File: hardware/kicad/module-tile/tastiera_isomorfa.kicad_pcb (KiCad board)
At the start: 2 copper layers, 63 parts, among them J101 Conn_LEFT, J102 Conn_TOP, J103 Conn_BOTTOM, J104 Conn_RIGHT, SW101 SW_Push, SW102 SW_Push, SW103 SW_Push, SW104 SW_Push, SW105 SW_Push, SW106 SW_Push, SW107 SW_Push, SW108 SW_Push, SW109 SW_Push, SW110 SW_Push, SW111 SW_Push, SW112 SW_Push, U101 74AUC2G126, U102 74AUC2G08, U103 74HC165, U104 74HC165, U105 74AHC1G04, U106 74LVC2G32, U107 74AUC2G125, U108 74LVC2G74, U109 74LS161

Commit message: Pcb started
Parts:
- C101, C102, C105, R101, R102, R103, R104, R105, R108, R109, R110, R111, R112, R113, R114, R115, R116, R117, R118, R119, R120, R121, R122, R123, R124, R125, R126, R127, R128, R129, R130, R131, R132, R133, U103, U104, U109: moved to B.Cu
- moved R113 167.6 mm to (174.2, 77.9), turned to 180 degrees
- moved R125 165.9 mm to (176.7, 70.9), turned to 90 degrees
- moved R117 161.0 mm to (184.2, 94.9), turned to 180 degrees
- moved R129 157.7 mm to (186.7, 88.4), turned to 90 degrees
- moved C104 153.2 mm to (128.3, 71.9), turned to 90 degrees
- moved R112 149.5 mm to (154.2, 77.9), turned to 180 degrees
- moved R121 149.5 mm to (174.2, 112.4), turned to 180 degrees
- moved U108 148.5 mm to (147.7, 75.4), turned to 90 degrees
- moved R124 148.3 mm to (156.7, 70.9), turned to 90 degrees
- moved C102 147.9 mm to (131.2, 82.9), turned to 90 degrees
- moved U104 146.7 mm to (124.6, 81.9), turned to -90 degrees
- moved R133 146.4 mm to (176.7, 105.4), turned to 90 degrees
- moved R115 136.6 mm to (144.2, 94.9), turned to 180 degrees
- moved R127 135.6 mm to (147.7, 88.9)
- moved J104 135.5 mm to (137.2, 86.8)
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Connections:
- U103 pad 3: /tile/BTNs11 -> /tile/keyboard/BTNs11
- U103 pad 4: /tile/BTNs10 -> /tile/keyboard/BTNs10
- U103 pad 5: /tile/BTNs9 -> /tile/keyboard/BTNs9
- U103 pad 6: /tile/BTNs8 -> /tile/keyboard/BTNs8
- U104 pad 11: /tile/BTNs7 -> /tile/keyboard/BTNs7
- U104 pad 12: /tile/BTNs6 -> /tile/keyboard/BTNs6
- U104 pad 13: /tile/BTNs5 -> /tile/keyboard/BTNs5
- U104 pad 14: /tile/BTNs4 -> /tile/keyboard/BTNs4
- U104 pad 3: /tile/BTNs3 -> /tile/keyboard/BTNs3
- U104 pad 4: /tile/BTNs2 -> /tile/keyboard/BTNs2
- U104 pad 5: /tile/BTNs1 -> /tile/keyboard/BTNs1
- U104 pad 6: /tile/BTNs0 -> /tile/keyboard/BTNs0
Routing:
- net /tile/keyboard/BTNs7: track 0.00 -> 99.5 mm
- net /tile/keyboard/BTNs6: track 0.00 -> 68.2 mm
- net /tile/keyboard/BTNs3: track 0.00 -> 59.5 mm
- net /tile/keyboard/BTNs2: track 0.00 -> 33.5 mm
- net /tile/keyboard/BTNs5: track 0.00 -> 27.4 mm
- net /tile/keyboard/BTNs4: track 0.00 -> 11.4 mm
- net /tile/keyboard/BTNs1: track 0.00 -> 9.48 mm
- net Net-(R110-Pad1): track 0.00 -> 8.02 mm
- net Net-(R113-Pad1): track 0.00 -> 8.02 mm
- net Net-(R112-Pad1): track 0.00 -> 8.02 mm
- net Net-(R111-Pad1): track 0.00 -> 8.02 mm
- net Net-(R118-Pad1): track 0.00 -> 7.94 mm
- net Net-(R121-Pad1): track 0.00 -> 7.94 mm
- net Net-(R120-Pad1): track 0.00 -> 7.94 mm
- net Net-(R119-Pad1): track 0.00 -> 7.94 mm
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
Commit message: First commit new branch
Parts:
- added J105: BTNs_L_MSB, Connector_PinSocket_2.54mm:PinSocket_1x08_P2.54mm_Vertical, F.Cu at (219.5, 129.8)
- added J106: BTNs_L_LSB, Connector_PinSocket_2.54mm:PinSocket_1x08_P2.54mm_Vertical, F.Cu at (179.5, 129.8)
- added J107: BTNs_MSB, Connector_PinHeader_2.54mm:PinHeader_1x08_P2.54mm_Vertical, B.Cu at (175.0, 54.4)
- added J108: BTNs_LSB, Connector_PinHeader_2.54mm:PinHeader_1x08_P2.54mm_Vertical, B.Cu at (135.0, 54.3)
- C101, C102, C105, R101, R102, R103, R104, R105, R108, R109, R122, R123, R124, R125, R126, R127, R128, R129, R130, R131, R132, R133, U103, U104, U109: moved to F.Cu
- J101: footprint Connector_PinHeader_2.54mm:PinHeader_1x06_P2.54mm_Vertical -> Connector_PinSocket_2.54mm:PinSocket_1x06_P2.54mm_Horizontal
- J102: footprint Connector_PinHeader_2.54mm:PinHeader_1x08_P2.54mm_Vertical -> Connector_PinSocket_2.54mm:PinSocket_1x08_P2.54mm_Horizontal
- J103: footprint Connector_PinHeader_2.54mm:PinHeader_1x08_P2.54mm_Vertical -> Connector_PinHeader_2.54mm:PinHeader_1x08_P2.54mm_Horizontal
- J104: footprint Connector_PinHeader_2.54mm:PinHeader_1x06_P2.54mm_Vertical -> Connector_PinHeader_2.54mm:PinHeader_1x06_P2.54mm_Horizontal
- moved C103 153.0 mm to (55.4, 180.2), turned to 0 degrees
- moved U108 151.7 mm to (38.7, 180.8), turned to 0 degrees
- moved U109 138.6 mm to (30.7, 184.4), turned to 0 degrees
- moved C104 133.3 mm to (55.4, 183.5), turned to 0 degrees
- moved C102 131.4 mm to (54.8, 189.7), turned to 0 degrees
- moved U106 129.2 mm to (97.3, 183.4), turned to 0 degrees
- moved R106 123.1 mm to (91.2, 176.5)
- moved R107 122.9 mm to (91.2, 179.5)
- moved C101 116.7 mm to (54.8, 186.7)
- moved R108 111.0 mm to (91.2, 182.4)
- moved R101 110.6 mm to (91.2, 161.8), turned to 0 degrees
- moved R102 110.3 mm to (91.2, 164.7)
- moved R104 108.5 mm to (91.2, 170.6), turned to 0 degrees
- moved U102 107.8 mm to (97.3, 178.8), turned to 0 degrees
- moved C105 107.6 mm to (47.2, 182.4), turned to 0 degrees
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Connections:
- R110 pad 2: /tile/keyboard/BTNs0 -> /keyboard/BTNs0
- R111 pad 2: /tile/keyboard/BTNs1 -> /keyboard/BTNs1
- R112 pad 2: /tile/keyboard/BTNs2 -> /keyboard/BTNs2
- R113 pad 2: /tile/keyboard/BTNs3 -> /keyboard/BTNs3
- R114 pad 2: /tile/keyboard/BTNs4 -> /keyboard/BTNs4
- R115 pad 2: /tile/keyboard/BTNs5 -> /keyboard/BTNs5
- R116 pad 2: /tile/keyboard/BTNs6 -> /keyboard/BTNs6
- R117 pad 2: /tile/keyboard/BTNs7 -> /keyboard/BTNs7
- R118 pad 2: /tile/keyboard/BTNs8 -> /keyboard/BTNs8
- R119 pad 2: /tile/keyboard/BTNs9 -> /keyboard/BTNs9
- R120 pad 2: /tile/keyboard/BTNs10 -> /keyboard/BTNs10
- R121 pad 2: /tile/keyboard/BTNs11 -> /keyboard/BTNs11
- R122 pad 2: GND -> GND_T
- R123 pad 2: GND -> GND_T
- R124 pad 2: GND -> GND_T
- R125 pad 2: GND -> GND_T
- R126 pad 2: GND -> GND_T
- R127 pad 2: GND -> GND_T
- R128 pad 2: GND -> GND_T
- R129 pad 2: GND -> GND_T
- R130 pad 2: GND -> GND_T
- R131 pad 2: GND -> GND_T
- R132 pad 2: GND -> GND_T
- R133 pad 2: GND -> GND_T
- SW101 pad 1: VCC -> VCC_T
- SW102 pad 1: VCC -> VCC_T
- SW103 pad 1: VCC -> VCC_T
- SW104 pad 1: VCC -> VCC_T
- SW105 pad 1: VCC -> VCC_T
- SW106 pad 1: VCC -> VCC_T
- SW107 pad 1: VCC -> VCC_T
- SW108 pad 1: VCC -> VCC_T
- SW109 pad 1: VCC -> VCC_T
- SW110 pad 1: VCC -> VCC_T
- SW111 pad 1: VCC -> VCC_T
- SW112 pad 1: VCC -> VCC_T
- U103 pad 3: /tile/keyboard/BTNs11 -> /tile/BTNs_L11
- U103 pad 4: /tile/keyboard/BTNs10 -> /tile/BTNs_L10
- U103 pad 5: /tile/keyboard/BTNs9 -> /tile/BTNs_L9
- U103 pad 6: /tile/keyboard/BTNs8 -> /tile/BTNs_L8
- U104 pad 11: /tile/keyboard/BTNs7 -> /tile/BTNs_L7
- U104 pad 12: /tile/keyboard/BTNs6 -> /tile/BTNs_L6
- U104 pad 13: /tile/keyboard/BTNs5 -> /tile/BTNs_L5
- U104 pad 14: /tile/keyboard/BTNs4 -> /tile/BTNs_L4
- U104 pad 3: /tile/keyboard/BTNs3 -> /tile/BTNs_L3
- U104 pad 4: /tile/keyboard/BTNs2 -> /tile/BTNs_L2
- U104 pad 5: /tile/keyboard/BTNs1 -> /tile/BTNs_L1
- U104 pad 6: /tile/keyboard/BTNs0 -> /tile/BTNs_L0
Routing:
- net VCC_T: track 0.00 -> 365.0 mm
- net GND_T: track 0.00 -> 141.9 mm
- net /tile/keyboard/BTNs7: track 99.5 -> 0.00 mm
- net /tile/keyboard/BTNs6: track 68.2 -> 0.00 mm
- net /tile/keyboard/BTNs3: track 59.5 -> 0.00 mm
- net /tile/keyboard/BTNs2: track 33.5 -> 0.00 mm
- net /keyboard/BTNs5: track 0.00 -> 28.4 mm
- net /keyboard/BTNs11: track 0.00 -> 28.4 mm
- net /tile/keyboard/BTNs5: track 27.4 -> 0.00 mm
- net /keyboard/BTNs7: track 0.00 -> 25.7 mm
- net /keyboard/BTNs1: track 0.00 -> 25.7 mm
- net Net-(R118-Pad1): track 7.94 -> 32.3 mm
- net /keyboard/BTNs4: track 0.00 -> 20.3 mm
- net /keyboard/BTNs10: track 0.00 -> 20.2 mm
- net Net-(R115-Pad1): track 5.05 -> 23.9 mm
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
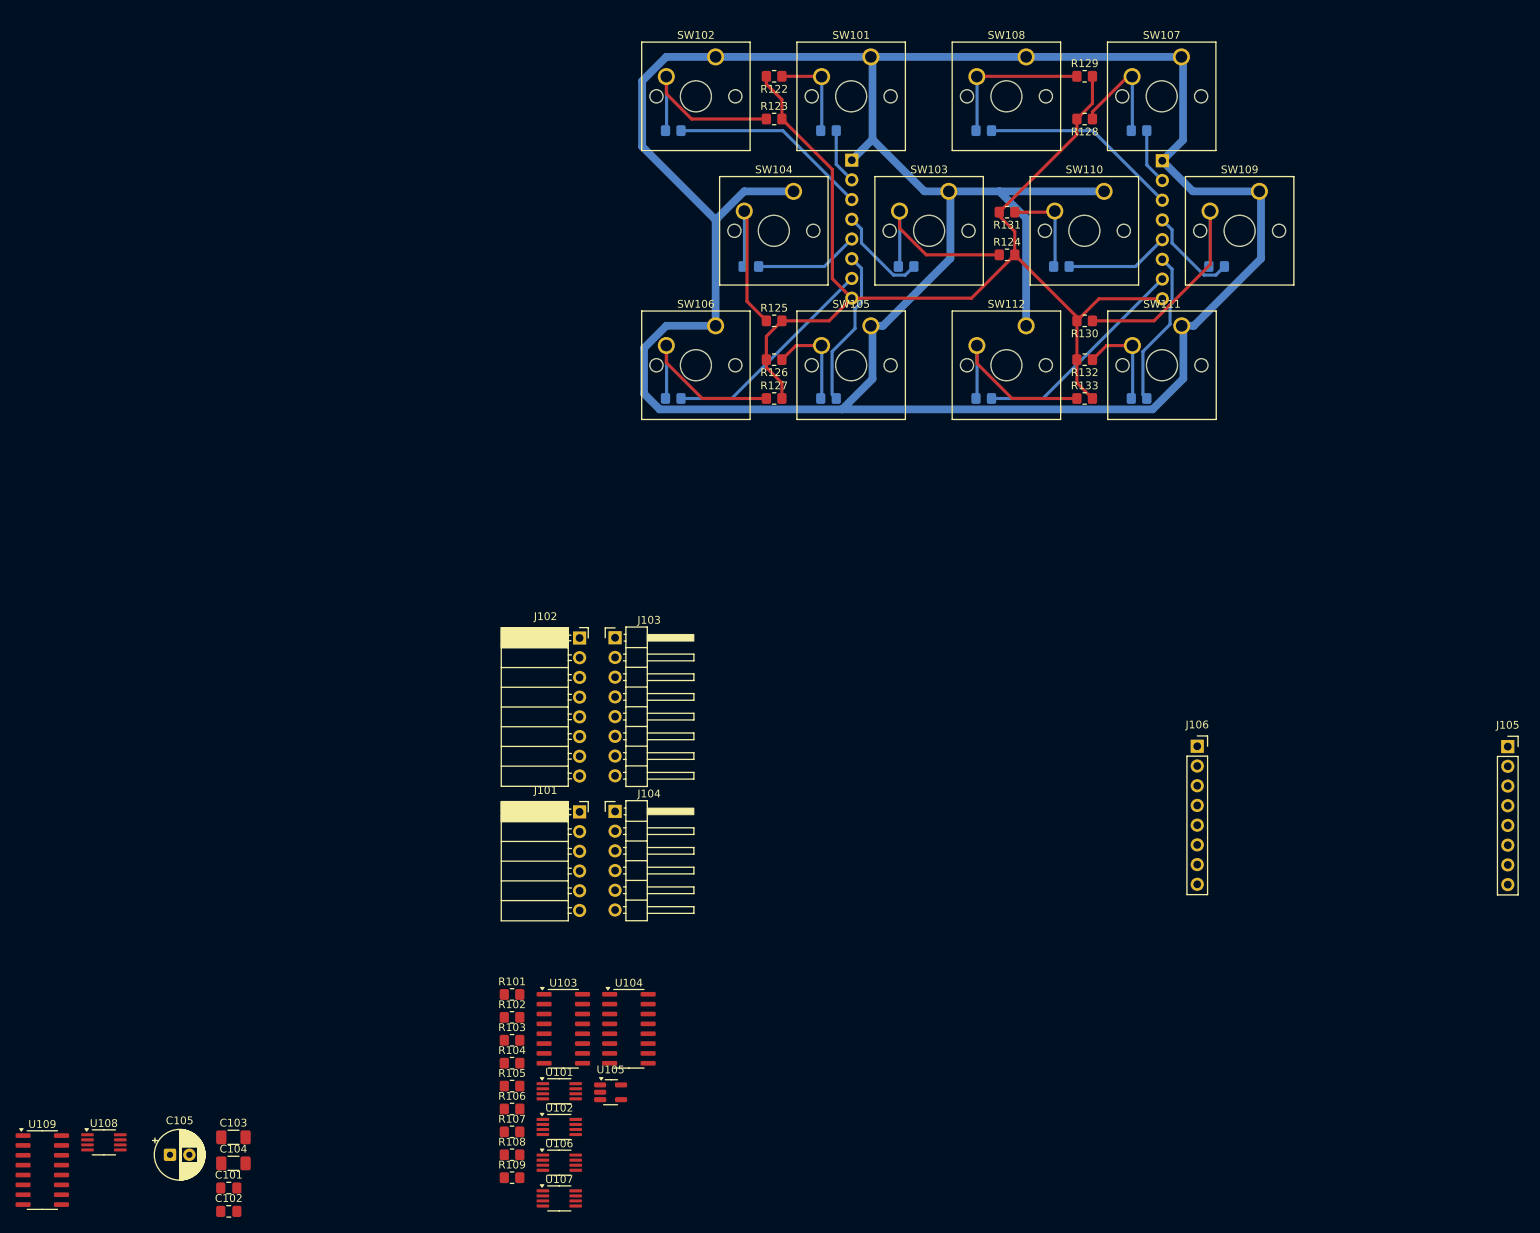
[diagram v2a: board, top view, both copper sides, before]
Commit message: Updated cpb with FreeRouting
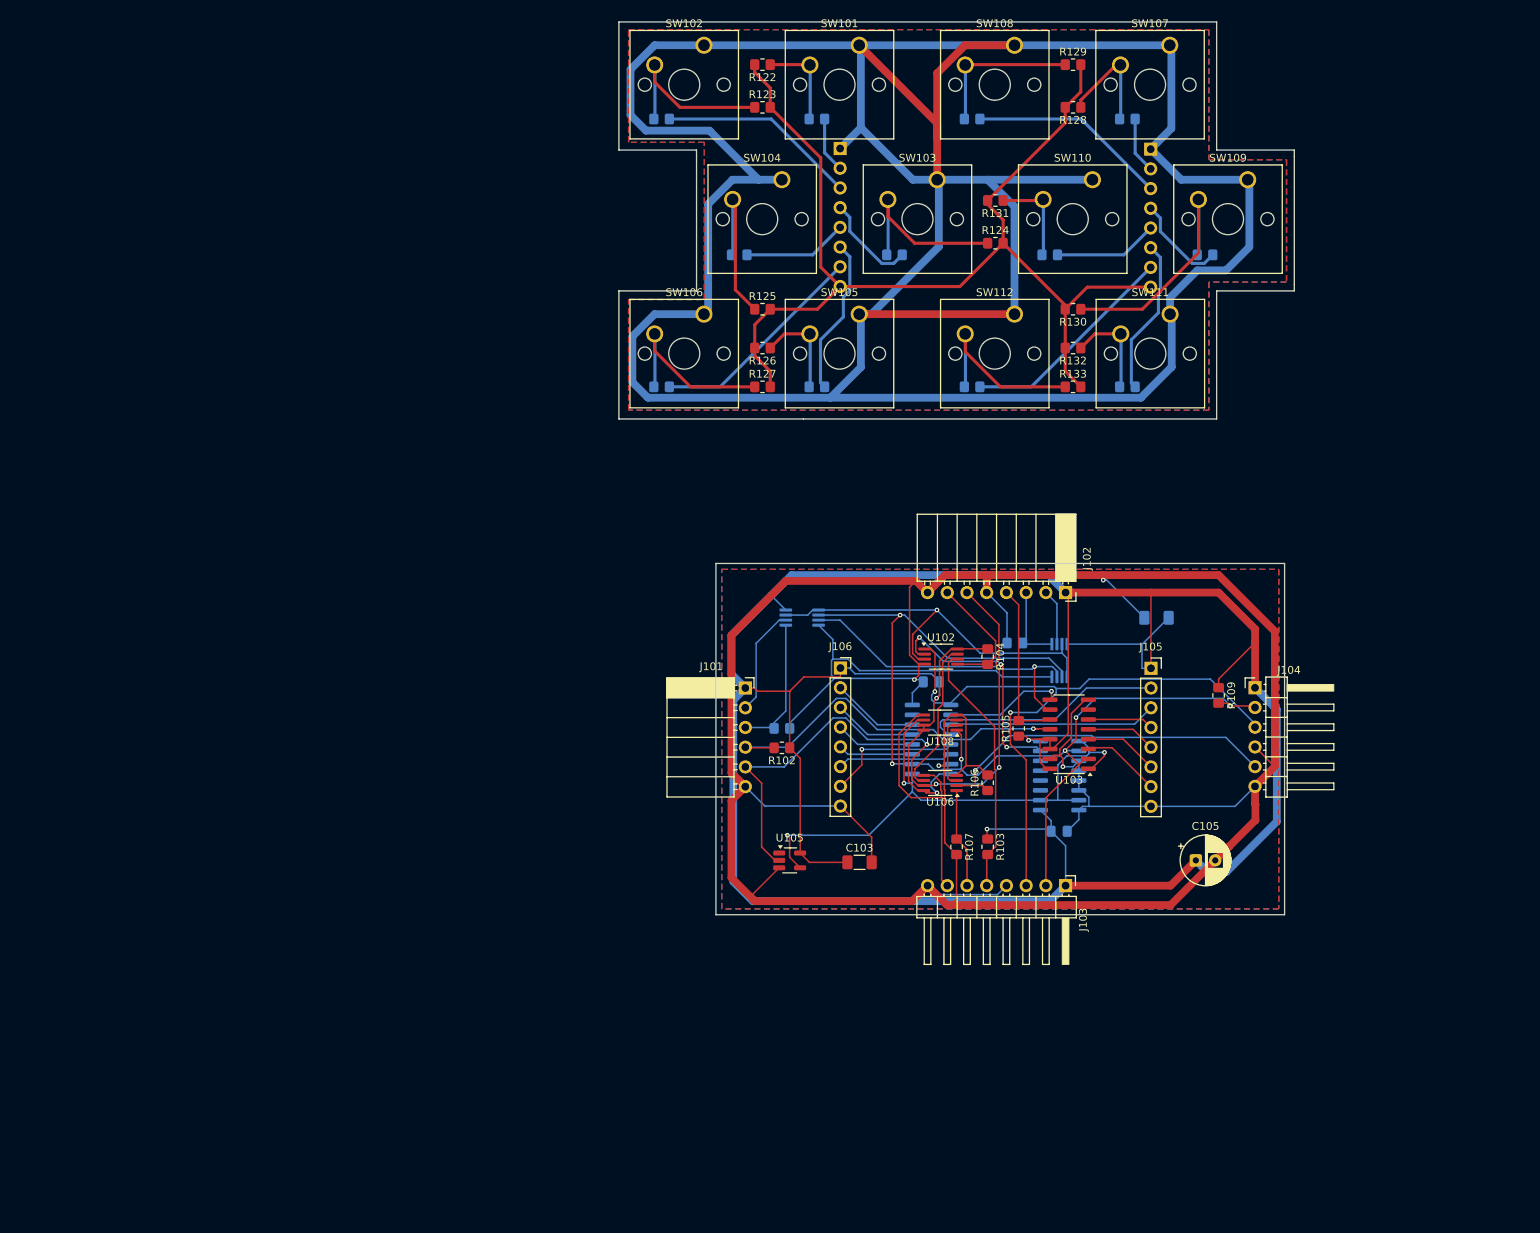
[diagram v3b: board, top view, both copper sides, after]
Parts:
- C101, C102, C104, R101, R108, U101, U104, U107, U109: moved to B.Cu
- moved U109 140.6 mm to (161.8, 133.6), turned to 180 degrees
- moved C104 138.1 mm to (174.2, 113.2), turned to 180 degrees
- moved C105 137.5 mm to (179.3, 144.5)
- moved U108 120.5 mm to (146.4, 126.8), turned to 180 degrees
- moved C101 116.4 mm to (161.7, 140.8)
- moved C102 113.3 mm to (145.2, 121.5), turned to 180 degrees
- moved R109 110.2 mm to (182.2, 123.2), turned to -90 degrees
- moved U107 94.6 mm to (161.8, 118.8), turned to 90 degrees
- moved R108 92.4 mm to (156.0, 116.5), turned to 180 degrees
- moved C103 88.1 mm to (136.0, 144.8)
- moved J104 84.0 mm to (186.9, 122.3)
- moved R104 80.6 mm to (152.5, 118.2), turned to -90 degrees
- moved R105 79.9 mm to (156.5, 127.5), turned to 90 degrees
- moved U102 78.0 mm to (146.5, 118.2)
- moved U103 75.4 mm to (163.0, 128.2), turned to 180 degrees
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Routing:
- net GND: track 0.00 -> 438.8 mm, vias 0 -> 4
- net VCC: track 0.00 -> 395.2 mm, vias 0 -> 4
- net /tile/B_clk: track 0.00 -> 138.9 mm, vias 0 -> 6
- net /tile/B_data: track 0.00 -> 84.8 mm, vias 0 -> 2
- net /tile/L_latch: track 0.00 -> 84.0 mm, vias 0 -> 3
- net /tile/counter/~{rst}: track 0.00 -> 75.0 mm, vias 0 -> 3
- net VCC_T: track 365.0 -> 431.6 mm
- net Net-(U101-Pad1): track 0.00 -> 51.4 mm, vias 0 -> 1
- net /tile/L_endrow: track 0.00 -> 51.0 mm, vias 0 -> 1
- net /tile/R_latch: track 0.00 -> 45.8 mm, vias 0 -> 1
- net Net-(U103-DS): track 0.00 -> 41.0 mm, vias 0 -> 1
- net Net-(U109-Tc): track 0.00 -> 33.8 mm, vias 0 -> 3
- net /tile/B_W: track 0.00 -> 33.2 mm
- net /tile/B_first: track 0.00 -> 33.1 mm
- net /tile/BTNs_L6: track 0.00 -> 31.3 mm
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- added copper zone on F.Cu, net GND
- added copper zone on F.Cu, net GND_T
- added copper zone on B.Cu, net VCC
- added copper zone on B.Cu, net VCC_T
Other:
- board outline added: 87 x 115 mm

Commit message: Design completed
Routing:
- net VCC_T: track 431.6 -> 113.7 mm
- net VCC: track 395.2 -> 285.6 mm
- net GND_T: track 141.9 -> 49.3 mm
- net GND: track 438.8 -> 409.7 mm, vias 4 -> 3
- net /tile/L_endrow: track 51.0 -> 48.4 mm
- net Net-(U109-Tc): track 33.8 -> 33.1 mm
- net /tile/B_W: track 33.2 -> 34.0 mm

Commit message: Upgrade
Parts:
- C104: moved to F.Cu
- moved U104 19.8 mm to (136.5, 111.2)
- moved U101 19.8 mm to (119.9, 95.5)
- moved C101 19.8 mm to (153.0, 123.0)
- moved C102 19.8 mm to (136.5, 103.8)
- moved C103 19.8 mm to (127.2, 127.0)
- moved C105 19.8 mm to (170.6, 126.8)
- moved J101 19.8 mm to (112.5, 104.5)
- moved J102 19.8 mm to (153.8, 92.2)
- moved J103 19.8 mm to (153.8, 130.0)
- moved J104 19.8 mm to (178.2, 104.5)
- moved J105 19.8 mm to (164.8, 102.0)
- moved R101 19.8 mm to (117.2, 109.8)
- moved R102 19.8 mm to (117.2, 112.2)
- moved R103 19.8 mm to (143.8, 125.0)
- moved R104 19.8 mm to (143.8, 100.5)
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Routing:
- net VCC: track 285.6 -> 261.8 mm
- net GND: track 409.7 -> 406.1 mm, vias 3 -> 2
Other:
- board size 87 x 115 mm -> 87 x 97.2 mm
- board text added: "A"
- board text added: "B"
- board text added: "Orturano Labs"
- board text added: "TORTIRE v0.1"
- board text added: "TORTIRE v0.1 Orturano Labs"
